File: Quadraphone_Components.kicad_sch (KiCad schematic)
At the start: 40 parts, among them J1 Conn_01x10_Male, J2 Conn_01x10_Male, J3 Conn_01x10_Male, J4 Conn_01x10_Male, J5 Eurorack_10_pin_power, Q1 MMBT3904, U1 AMS1117-5.0, U14 LM4040DBZ-2.5, U3 MCP6002, U4 LM4040DBZ-5, U5 MCP6004, U8 74LV4066PW

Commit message: Updates for v3 production
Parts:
- TP1, TP2, TP3, TP4, TP5, TP6, TP7, TP8: now left out of the parts list
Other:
- note added: "Rev 2.0: Added startup synch pulse circuit Rev 3.0: Remove jumper R5; Separate buffer for PWM opamp power - Change mix output feedback resistor from 36k to 30k to decrease output - Synch switch leaks in off position"
- note removed: "Rev 2.0: Added startup synch pulse circuit Rev 3.0: Remove jumper R5; Separate buffer for PWM opamp power"

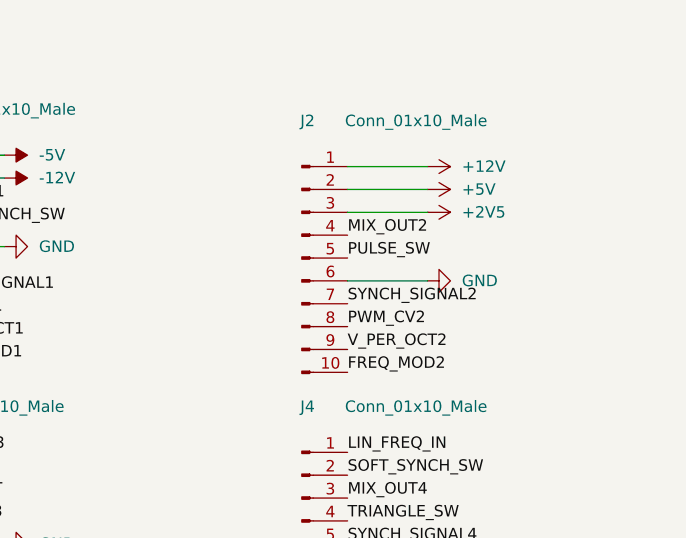
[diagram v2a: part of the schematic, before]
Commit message: Updated resistor values in VCO tuning circuits
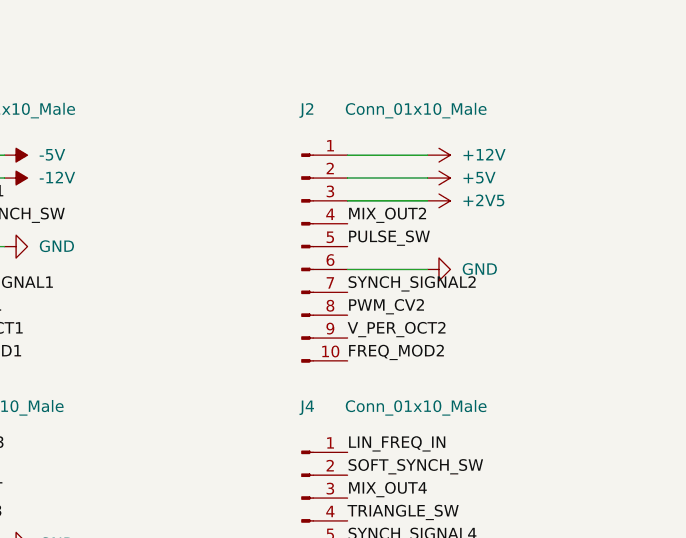
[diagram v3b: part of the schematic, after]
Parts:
- C11: Part_Number C134798 -> (none); Rotation 360 -> (none)
- C12: Part_Number C134793 -> (none); Rotation 270 -> (none)
- D1, D2: Part_Number C8598 -> (none)
- J1, J2, J3, J4: now left out of the parts list
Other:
- moved on the sheet: J2
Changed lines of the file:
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@@
     (stroke (width 0) (type default))
   )
-  (wire (pts (xy 257.81 30.48) (xy 248.92 30.48))
+  (wire (pts (xy 257.81 29.21) (xy 248.92 29.21))
     (stroke (width 0) (type default))
   )
@@
     (stroke (width 0) (type default))
   )
-  (wire (pts (xy 257.81 40.64) (xy 248.92 40.64))
+  (wire (pts (xy 257.81 39.37) (xy 248.92 39.37))
     (stroke (width 0) (type default))
   )
@@
     (stroke (width 0) (type default))
   )
-  (wire (pts (xy 257.81 33.02) (xy 248.92 33.02))
+  (wire (pts (xy 257.81 31.75) (xy 248.92 31.75))
     (stroke (width 0) (type default))
   )
@@
     (stroke (width 0) (type default))
   )
-  (wire (pts (xy 257.81 27.94) (xy 248.92 27.94))
+  (wire (pts (xy 257.81 26.67) (xy 248.92 26.67))
     (stroke (width 0) (type default))
   )
@@
     (effects (font (size 1.27 1.27)) (justify right bottom))
   )
-  (label "SYNCH_SIGNAL2" (at 248.92 43.18 0) (fields_autoplaced)
+  (label "SYNCH_SIGNAL2" (at 248.92 41.91 0) (fields_autoplaced)
     (effects (font (size 1.27 1.27)) (justify left bottom))
   )
@@
     (effects (font (size 1.27 1.27)) (justify right bottom))
   )
-  (label "PULSE_SW" (at 248.92 38.1 0) (fields_autoplaced)
+  (label "PULSE_SW" (at 248.92 36.83 0) (fields_autoplaced)
     (effects (font (size 1.27 1.27)) (justify left bottom))
   )
@@
     (effects (font (size 1.27 1.27)) (justify right bottom))
   )
-  (label "PWM_CV2" (at 248.92 45.72 0) (fields_autoplaced)
+  (label "PWM_CV2" (at 248.92 44.45 0) (fields_autoplaced)
     (effects (font (size 1.27 1.27)) (justify left bottom))
   )
-  (label "MIX_OUT2" (at 248.92 35.56 0) (fields_autoplaced)
+  (label "MIX_OUT2" (at 248.92 34.29 0) (fields_autoplaced)
     (effects (font (size 1.27 1.27)) (justify left bottom))
   )
@@
     (effects (font (size 1.27 1.27)) (justify right bottom))
   )
-  (label "FREQ_MOD2" (at 248.92 50.8 0) (fields_autoplaced)
+  (label "FREQ_MOD2" (at 248.92 49.53 0) (fields_autoplaced)
     (effects (font (size 1.27 1.27)) (justify left bottom))
   )
@@
     (effects (font (size 1.27 1.27)) (justify right bottom))
   )
-  (label "V_PER_OCT2" (at 248.92 48.26 0) (fields_autoplaced)
+  (label "V_PER_OCT2" (at 248.92 46.99 0) (fields_autoplaced)
     (effects (font (size 1.27 1.27)) (justify left bottom))
   )
@@
     )
   )
-  (symbol (lib_id "power:GND") (at 257.81 40.64 90) (unit 1)
+  (symbol (lib_id "power:GND") (at 257.81 39.37 90) (unit 1)
     (in_bom yes) (on_board yes) (dnp no) (fields_autoplaced)
-    (property "Reference" "#PWR018" (at 264.16 40.64 0)
+    (property "Reference" "#PWR018" (at 264.16 39.37 0)
       (effects (font (size 1.27 1.27)) hide)
     )
-    (property "Value" "GND" (at 261.62 40.6399 90)
+    (property "Value" "GND" (at 261.62 39.3699 90)
       (effects (font (size 1.27 1.27)) (justify right))
     )
-    (property "Footprint" "" (at 257.81 40.64 0)
+    (property "Footprint" "" (at 257.81 39.37 0)
       (effects (font (size 1.27 1.27)) hide)
     )
-    (property "Datasheet" "" (at 257.81 40.64 0)
+    (property "Datasheet" "" (at 257.81 39.37 0)
       (effects (font (size 1.27 1.27)) hide)
     )
@@
       (effects (font (size 1.27 1.27)) hide)
     )
-    (property "Part_Number" "C134798" (at 36.83 125.73 0)
-      (effects (font (size 1.27 1.27)) hide)
-    )
-    (property "Rotation" "360" (at 36.83 125.73 0)
-      (effects (font (size 1.27 1.27)) hide)
-    )
     (pin "1")
     (pin "2")
@@
     )
   )
-  (symbol (lib_id "power:+2V5") (at 257.81 33.02 270) (unit 1)
+  (symbol (lib_id "power:+2V5") (at 257.81 31.75 270) (unit 1)
     (in_bom yes) (on_board yes) (dnp no) (fields_autoplaced)
-    (property "Reference" "#PWR019" (at 254 33.02 0)
+    (property "Reference" "#PWR019" (at 254 31.75 0)
       (effects (font (size 1.27 1.27)) hide)
     )
-    (property "Value" "+2V5" (at 261.62 33.0199 90)
+    (property "Value" "+2V5" (at 261.62 31.7499 90)
       (effects (font (size 1.27 1.27)) (justify left))
     )
-    (property "Footprint" "" (at 257.81 33.02 0)
+    (property "Footprint" "" (at 257.81 31.75 0)
       (effects (font (size 1.27 1.27)) hide)
     )
-    (property "Datasheet" "" (at 257.81 33.02 0)
+    (property "Datasheet" "" (at 257.81 31.75 0)
       (effects (font (size 1.27 1.27)) hide)
     )
@@
   )
   (symbol (lib_id "Connector:Conn_01x10_Male") (at 196.85 69.85 0) (unit 1)
-    (in_bom yes) (on_board yes) (dnp no)
+    (in_bom no) (on_board yes) (dnp no)
     (property "Reference" "J3" (at 197.485 54.61 0)
       (effects (font (size 1.27 1.27)))
@@
     )
   )
-  (symbol (lib_id "Connector:Conn_01x10_Male") (at 243.84 38.1 0) (unit 1)
-    (in_bom yes) (on_board yes) (dnp no)
-    (property "Reference" "J2" (at 244.475 22.86 0)
+  (symbol (lib_id "Connector:Conn_01x10_Male") (at 243.84 36.83 0) (unit 1)
+    (in_bom no) (on_board yes) (dnp no)
+    (property "Reference" "J2" (at 244.475 21.59 0)
       (effects (font (size 1.27 1.27)))
     )
-    (property "Value" "Conn_01x10_Male" (at 256.54 22.86 0)
+    (property "Value" "Conn_01x10_Male" (at 256.54 21.59 0)
       (effects (font (size 1.27 1.27)))
     )
-    (property "Footprint" "Connector_PinHeader_2.54mm:PinHeader_1x10_P2.54mm_Vertical" (at 243.84 38.1 0)
+    (property "Footprint" "Connector_PinHeader_2.54mm:PinHeader_1x10_P2.54mm_Vertical" (at 243.84 36.83 0)
       (effects (font (size 1.27 1.27)) hide)
     )
-    (property "Datasheet" "~" (at 243.84 38.1 0)
+    (property "Datasheet" "~" (at 243.84 36.83 0)
       (effects (font (size 1.27 1.27)) hide)
     )
@@
       (effects (font (size 1.27 1.27)) hide)
     )
-    (property "Part_Number" "C134793" (at 36.83 151.13 0)
-      (effects (font (size 1.27 1.27)) hide)
-    )
-    (property "Rotation" "270" (at 36.83 151.13 0)
-      (effects (font (size 1.27 1.27)) hide)
-    )
     (pin "1")
     (pin "2")
@@
     )
   )
-  (symbol (lib_id "power:+12V") (at 257.81 27.94 270) (mirror x) (unit 1)
+  (symbol (lib_id "power:+12V") (at 257.81 26.67 270) (mirror x) (unit 1)
     (in_bom yes) (on_board yes) (dnp no) (fields_autoplaced)
-    (property "Reference" "#PWR039" (at 254 27.94 0)
+    (property "Reference" "#PWR039" (at 254 26.67 0)
       (effects (font (size 1.27 1.27)) hide)
     )
-    (property "Value" "+12V" (at 261.62 27.9399 90)
+    (property "Value" "+12V" (at 261.62 26.6699 90)
       (effects (font (size 1.27 1.27)) (justify left))
     )
-    (property "Footprint" "" (at 257.81 27.94 0)
+    (property "Footprint" "" (at 257.81 26.67 0)
       (effects (font (size 1.27 1.27)) hide)
     )
-    (property "Datasheet" "" (at 257.81 27.94 0)
+    (property "Datasheet" "" (at 257.81 26.67 0)
       (effects (font (size 1.27 1.27)) hide)
     )
@@
       (effects (font (size 1.27 1.27)) hide)
     )
-    (property "Part_Number" "C8598" (at 48.26 144.78 0)
-      (effects (font (size 1.27 1.27)) hide)
-    )
     (pin "1")
     (pin "2")
@@
     )
   )
-  (symbol (lib_id "power:+5V") (at 257.81 30.48 270) (unit 1)
+  (symbol (lib_id "power:+5V") (at 257.81 29.21 270) (unit 1)
     (in_bom yes) (on_board yes) (dnp no) (fields_autoplaced)
-    (property "Reference" "#PWR020" (at 254 30.48 0)
+    (property "Reference" "#PWR020" (at 254 29.21 0)
       (effects (font (size 1.27 1.27)) hide)
     )
-    (property "Value" "+5V" (at 261.62 30.4799 90)
+    (property "Value" "+5V" (at 261.62 29.2099 90)
       (effects (font (size 1.27 1.27)) (justify left))
     )
-    (property "Footprint" "" (at 257.81 30.48 0)
+    (property "Footprint" "" (at 257.81 29.21 0)
       (effects (font (size 1.27 1.27)) hide)
     )
-    (property "Datasheet" "" (at 257.81 30.48 0)
+    (property "Datasheet" "" (at 257.81 29.21 0)
       (effects (font (size 1.27 1.27)) hide)
     )
@@
   )
   (symbol (lib_id "Connector:Conn_01x10_Male") (at 243.84 69.85 0) (unit 1)
-    (in_bom yes) (on_board yes) (dnp no)
+    (in_bom no) (on_board yes) (dnp no)
     (property "Reference" "J4" (at 244.475 54.61 0)
       (effects (font (size 1.27 1.27)))
@@
       (effects (font (size 1.27 1.27)) hide)
     )
-    (property "Part_Number" "C8598" (at 48.26 134.62 0)
-      (effects (font (size 1.27 1.27)) hide)
-    )
     (pin "1")
     (pin "2")
@@
   )
   (symbol (lib_id "Connector:Conn_01x10_Male") (at 196.85 36.83 0) (unit 1)
-    (in_bom yes) (on_board yes) (dnp no)
+    (in_bom no) (on_board yes) (dnp no)
     (property "Reference" "J1" (at 197.485 21.59 0)
       (effects (font (size 1.27 1.27)))

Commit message: Gerbers Prepared and Ordered
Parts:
- J1, J2, J3, J4: symbol Connector:Conn_01x10_Male -> Connector:Conn_01x10_Pin; now in the parts list
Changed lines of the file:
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@@
     )
   )
-  (symbol (lib_id "Connector:Conn_01x10_Male") (at 196.85 69.85 0) (unit 1)
-    (in_bom no) (on_board yes) (dnp no)
+  (symbol (lib_id "Connector:Conn_01x10_Pin") (at 196.85 69.85 0) (unit 1)
+    (in_bom yes) (on_board yes) (dnp no)
     (property "Reference" "J3" (at 197.485 54.61 0)
       (effects (font (size 1.27 1.27)))
@@
     )
   )
-  (symbol (lib_id "Connector:Conn_01x10_Male") (at 243.84 36.83 0) (unit 1)
-    (in_bom no) (on_board yes) (dnp no)
+  (symbol (lib_id "Connector:Conn_01x10_Pin") (at 243.84 36.83 0) (unit 1)
+    (in_bom yes) (on_board yes) (dnp no)
     (property "Reference" "J2" (at 244.475 21.59 0)
       (effects (font (size 1.27 1.27)))
@@
       (effects (font (size 1.27 1.27) italic) (justify left) hide)
     )
-    (property "Datasheet" "https://www.onsemi.com/pub/Collateral/2N3903-D.PDF" (at 256.54 135.89 0)
+    (property "Datasheet" "https://www.onsemi.com/pdf/datasheet/pzt3904-d.pdf" (at 256.54 135.89 0)
       (effects (font (size 1.27 1.27)) (justify left) hide)
     )
@@
     )
   )
-  (symbol (lib_id "Connector:Conn_01x10_Male") (at 243.84 69.85 0) (unit 1)
-    (in_bom no) (on_board yes) (dnp no)
+  (symbol (lib_id "Connector:Conn_01x10_Pin") (at 243.84 69.85 0) (unit 1)
+    (in_bom yes) (on_board yes) (dnp no)
     (property "Reference" "J4" (at 244.475 54.61 0)
       (effects (font (size 1.27 1.27)))
@@
     )
   )
-  (symbol (lib_id "Connector:Conn_01x10_Male") (at 196.85 36.83 0) (unit 1)
-    (in_bom no) (on_board yes) (dnp no)
+  (symbol (lib_id "Connector:Conn_01x10_Pin") (at 196.85 36.83 0) (unit 1)
+    (in_bom yes) (on_board yes) (dnp no)
     (property "Reference" "J1" (at 197.485 21.59 0)
       (effects (font (size 1.27 1.27)))
